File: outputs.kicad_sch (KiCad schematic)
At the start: 6 parts, among them U2 VNLD5160TR-E, U3 VNLD5160TR-E

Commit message: still initial layout
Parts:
- R3, R4, R5, R6: footprint (none) -> Resistor_SMD:R_0402_1005Metric
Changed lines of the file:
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@@
 			)
 		)
-		(property "Footprint" ""
+		(property "Footprint" "Resistor_SMD:R_0402_1005Metric"
 			(at 40.64 95.25 0)
 			(effects
@@
 			)
 		)
-		(property "Footprint" ""
+		(property "Footprint" "Resistor_SMD:R_0402_1005Metric"
 			(at 40.64 55.88 0)
 			(effects
@@
 			)
 		)
-		(property "Footprint" ""
+		(property "Footprint" "Resistor_SMD:R_0402_1005Metric"
 			(at 40.64 105.41 0)
 			(effects
@@
 			)
 		)
-		(property "Footprint" ""
+		(property "Footprint" "Resistor_SMD:R_0402_1005Metric"
 			(at 40.64 45.72 0)
 			(effects

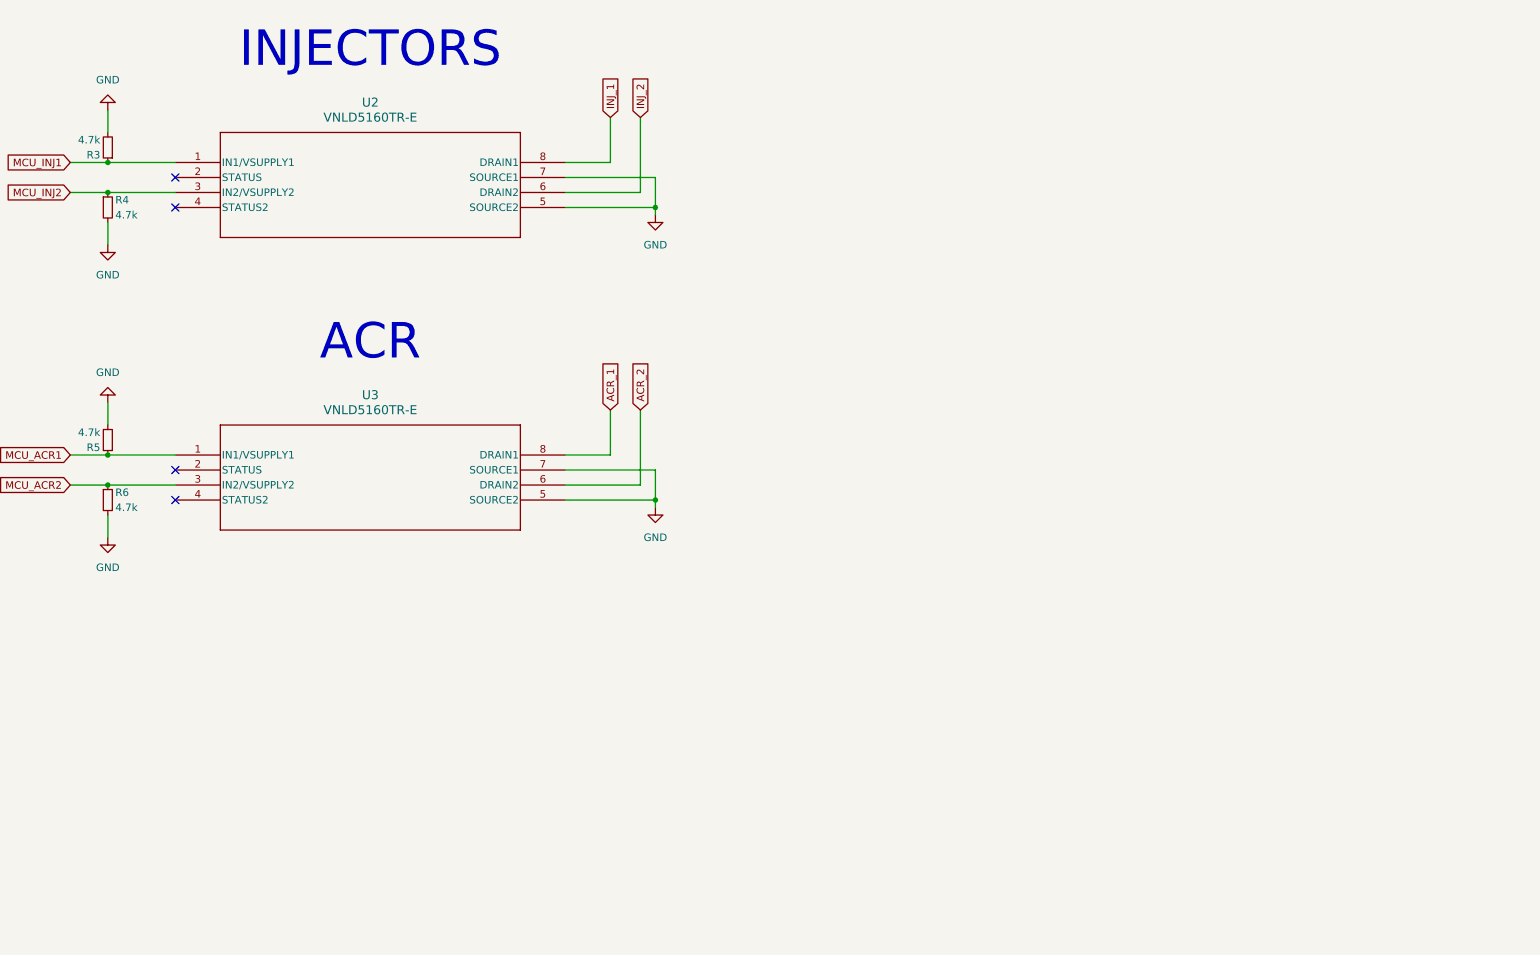
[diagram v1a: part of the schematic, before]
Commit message: igntion igbt, cooling mosfet
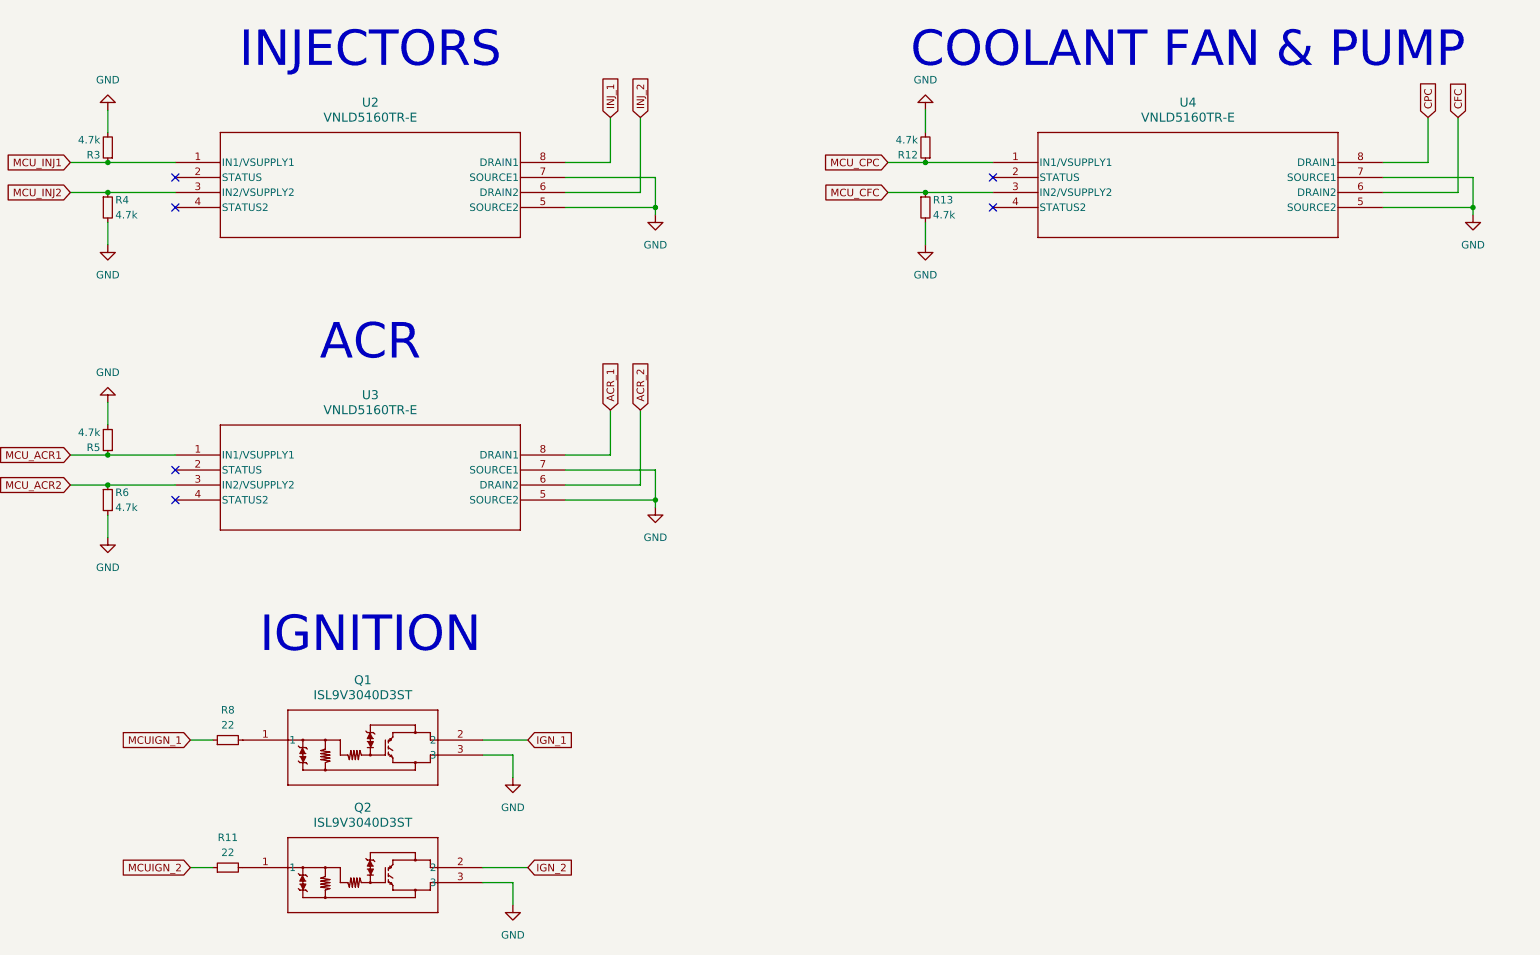
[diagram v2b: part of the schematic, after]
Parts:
- added Q1, Q2: ISL9V3040D3ST, TO-252AA_ONS, symbol ISL9V3040D3ST:ISL9V3040D3ST
- added R11, R8: 22, Resistor_SMD:R_0603_1608Metric, symbol Device:R_Small
- added R12, R13: 4.7k, Resistor_SMD:R_0402_1005Metric, symbol Device:R_Small
- added U4: VNLD5160TR-E, VNLD5160TR-E:SO_160TR-E_STM, symbol VNLD5160TR-E:VNLD5160TR-E
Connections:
- net GND: now also Q1.3, Q2.3, R12.2, R13.2, U4.5 (SOURCE2), U4.7 (SOURCE1)
- new net: Q2.1, R11.2
- new net: Q1.1, R8.2
- new net CFC: U4.6 (DRAIN2)
- new net CPC: U4.8 (DRAIN1)
- new net IGN_1: Q1.2
- new net IGN_2: Q2.2
- new net MCUIGN_1: R8.1
- new net MCUIGN_2: R11.1
- new net MCU_CFC: R13.1, U4.3 (IN2/VSUPPLY2)
- new net MCU_CPC: R12.1, U4.1 (IN1/VSUPPLY1)
- no-connect marks 4 -> 6
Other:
- note added: "COOLANT FAN & PUMP"
- note added: "IGNITION"

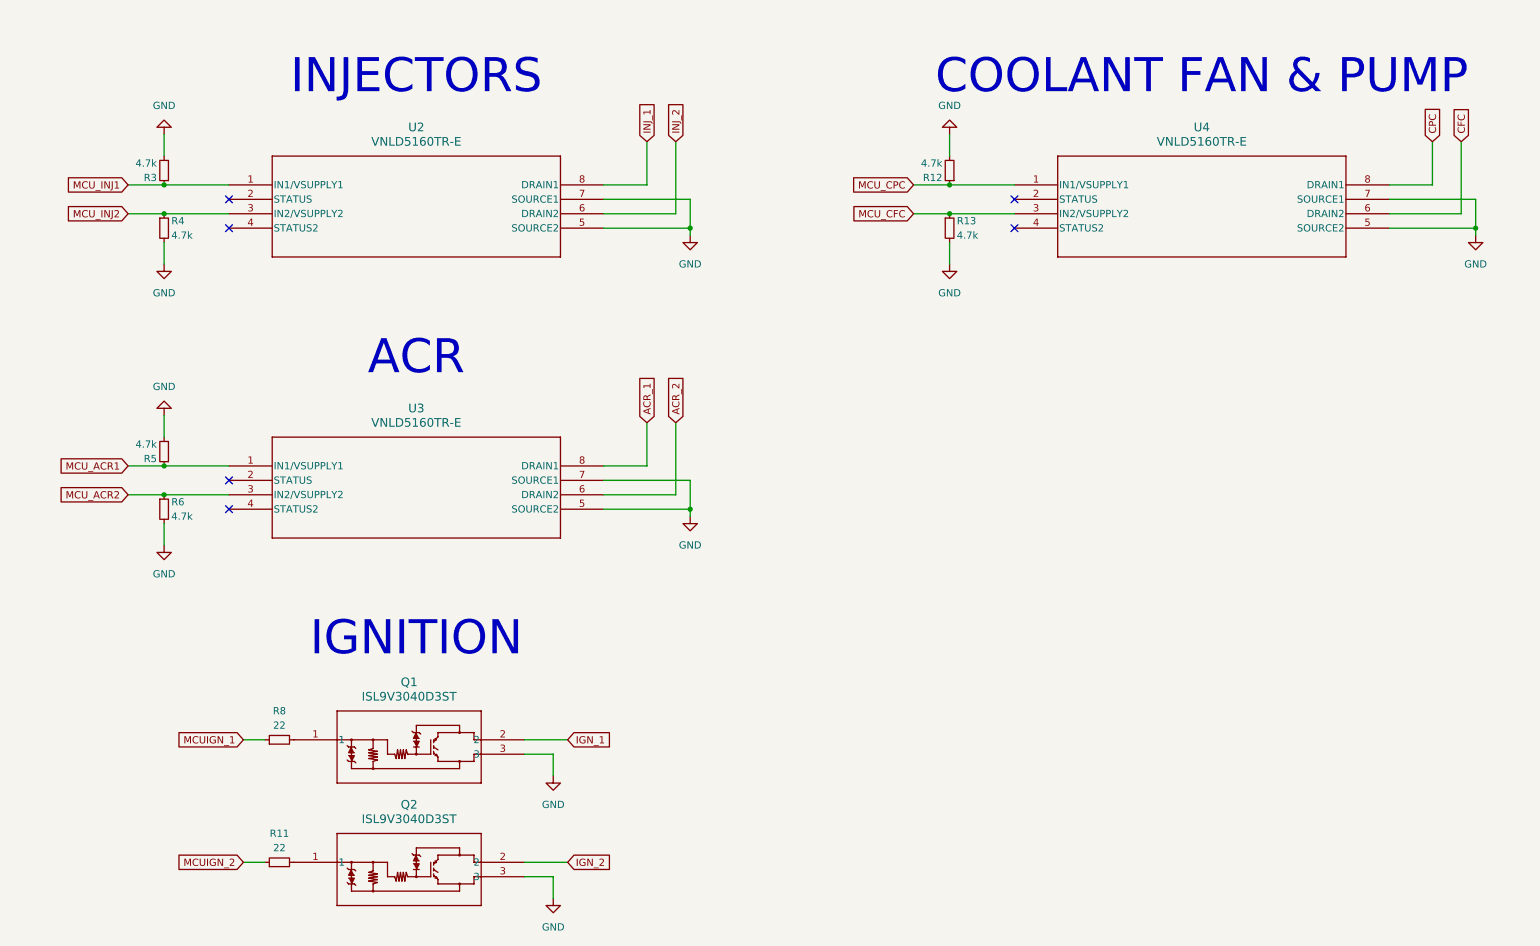
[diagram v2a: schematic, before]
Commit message: adding electronic throttle control
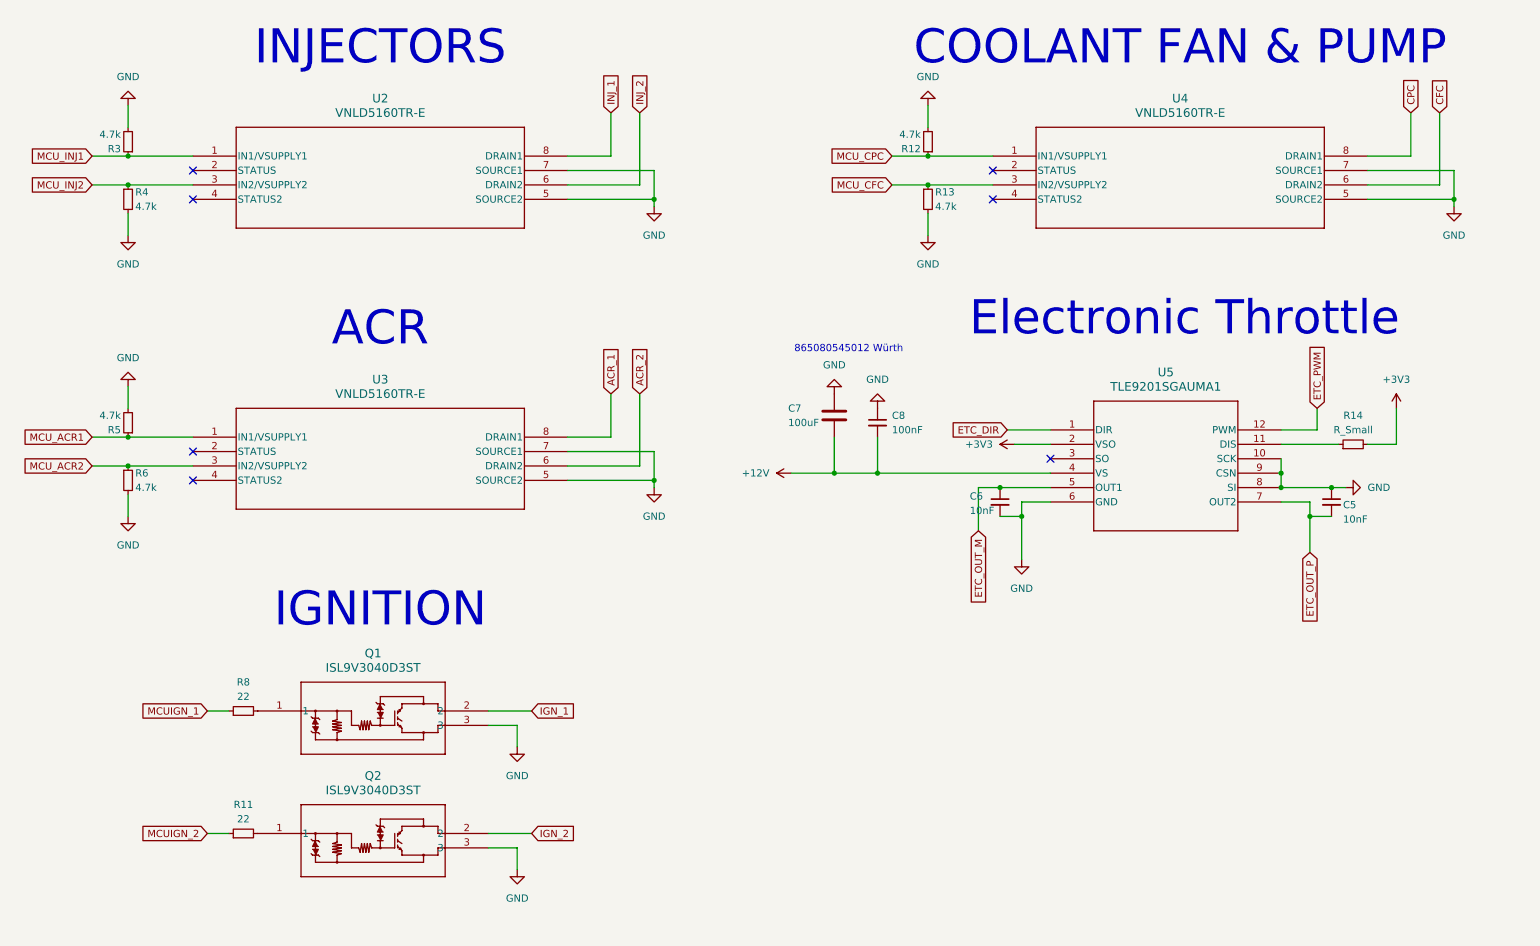
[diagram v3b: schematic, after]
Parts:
- added C5, C6: 10nF, Capacitor_SMD:C_0402_1005Metric, symbol Device:C_Small
- added C7: 100uF, Capacitor_SMD:C_Elec_6.3x5.8, symbol Device:C
- added C8: 100nF, Capacitor_SMD:C_0603_1608Metric, symbol Device:C_Small
- added R14: R_Small, symbol Device:R_Small
- added U5: TLE9201SGAUMA1, TLE9201SG:TLE9201SGAUMA1_INF, symbol TLE9201SG:TLE9201SGAUMA1
- Q1, Q2: footprint TO-252AA_ONS -> ISL9V3040D3ST:TO-252AA_ONS
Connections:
- net GND: now also C5.1, C6.2, C7.1, C8.1, U5.10 (SCK), U5.6 (GND), U5.8 (SI), U5.9 (CSN)
- new net: R14.1, U5.11 (DIS)
- new net +12V: C7.2, C8.2, U5.4 (VS)
- new net +3V3: R14.2, U5.2 (VSO)
- new net ETC_DIR: U5.1 (DIR)
- new net ETC_OUT_M: C6.1, U5.5 (OUT1)
- new net ETC_OUT_P: C5.2, U5.7 (OUT2)
- new net ETC_PWM: U5.12 (PWM)
- no-connect marks 6 -> 7
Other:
- note added: "865080545012 Würth"
- note added: "Electronic Throttle"
- moved on the sheet: Q1, Q2, R11, R12, R13, R3, R4, R5, R6, R8, U2, U3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

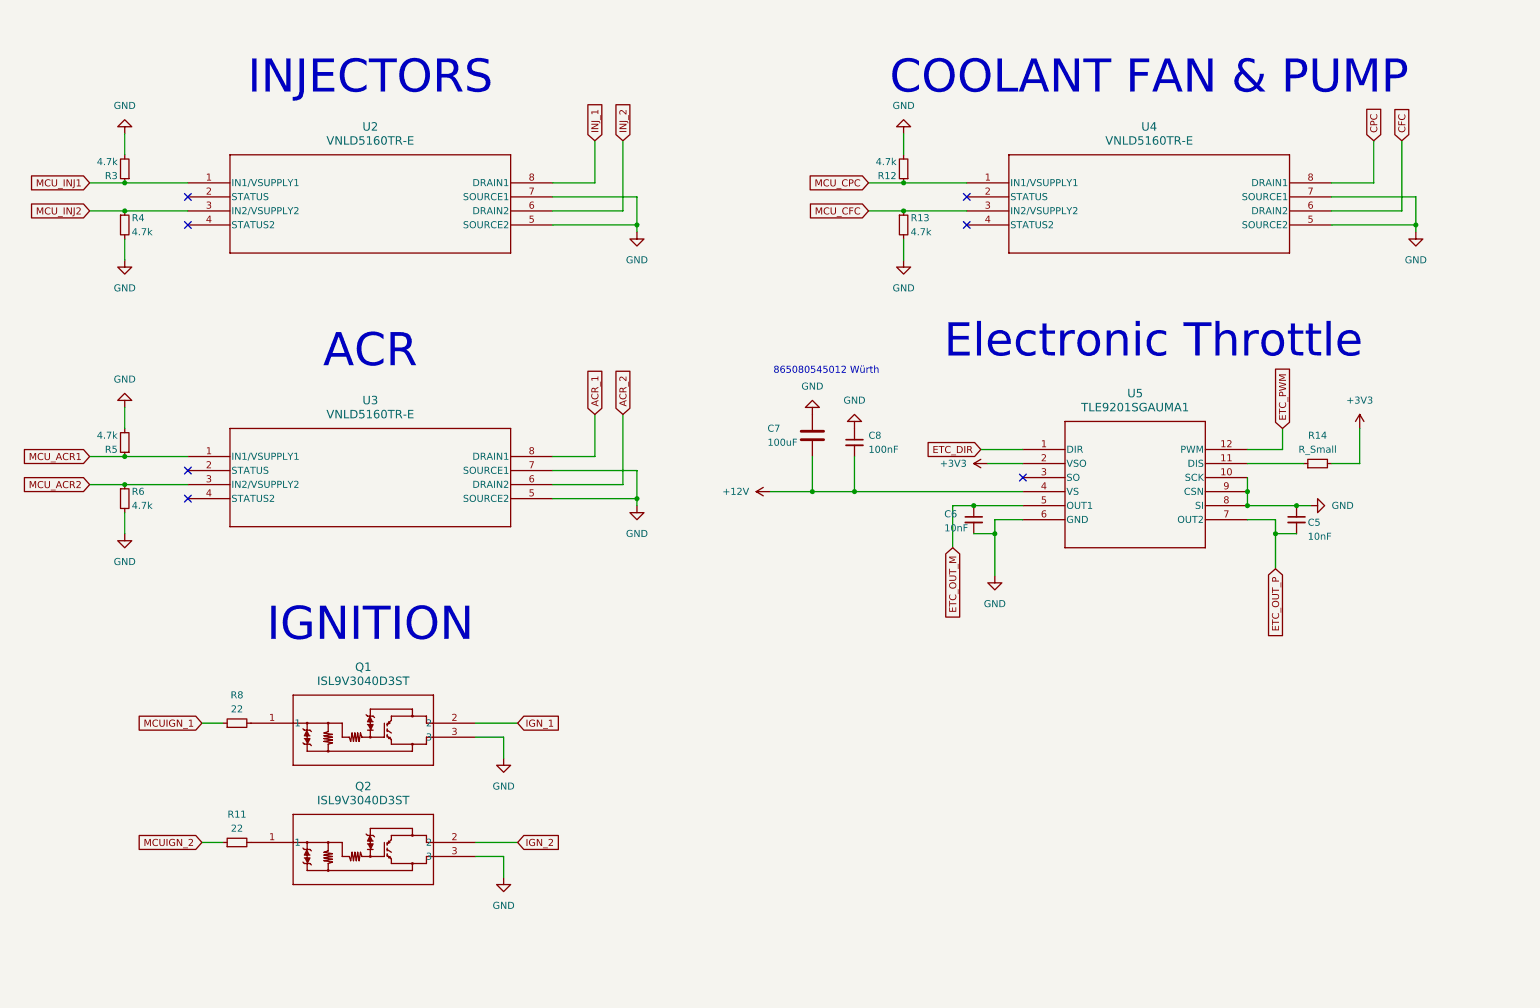
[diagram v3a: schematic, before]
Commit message: adding most remaining outputs and sensors like vvt, cam etc
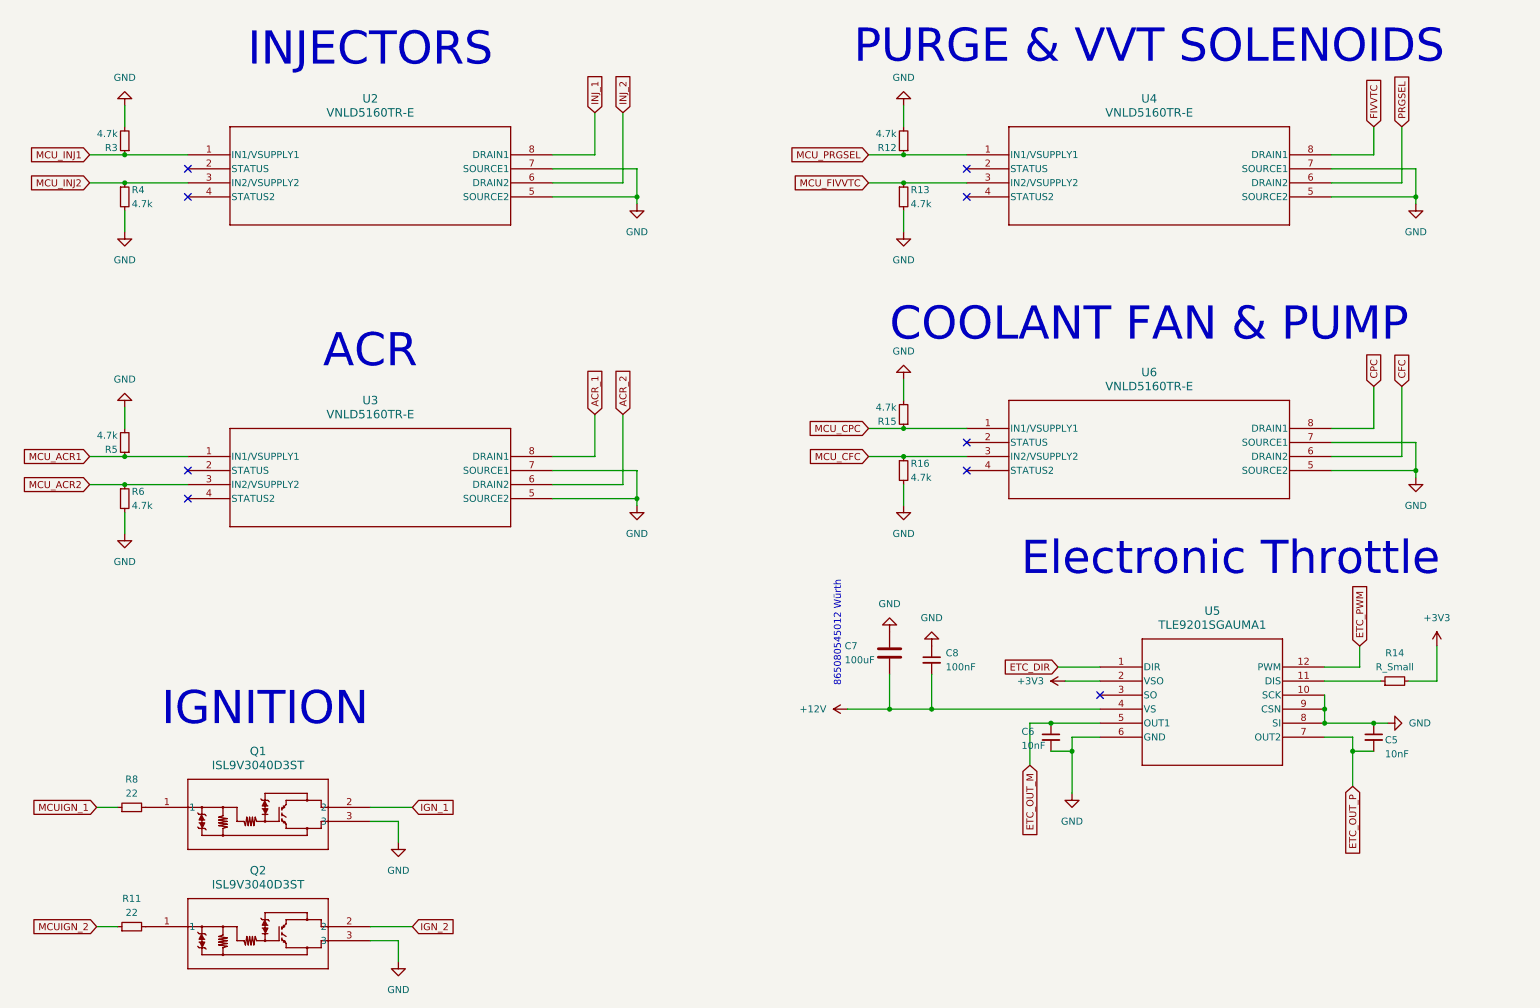
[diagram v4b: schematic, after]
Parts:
- added R15, R16: 4.7k, Resistor_SMD:R_0402_1005Metric, symbol Device:R_Small
- added U6: VNLD5160TR-E, VNLD5160TR-E:SO_160TR-E_STM, symbol VNLD5160TR-E:VNLD5160TR-E
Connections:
- net CFC: now also U6.6 (DRAIN2); no longer U4.6 (DRAIN2)
- net CPC: now also U6.8 (DRAIN1); no longer U4.8 (DRAIN1)
- net GND: now also R15.2, R16.2, U6.5 (SOURCE2), U6.7 (SOURCE1)
- net MCU_CFC: now also R16.1, U6.3 (IN2/VSUPPLY2); no longer R13.1, U4.3 (IN2/VSUPPLY2)
- net MCU_CPC: now also R15.1, U6.1 (IN1/VSUPPLY1); no longer R12.1, U4.1 (IN1/VSUPPLY1)
- new net FIVVTC: U4.8 (DRAIN1)
- new net MCU_FIVVTC: R13.1, U4.3 (IN2/VSUPPLY2)
- new net MCU_PRGSEL: R12.1, U4.1 (IN1/VSUPPLY1)
- new net PRGSEL: U4.6 (DRAIN2)
- no-connect marks 7 -> 9
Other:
- note added: "PURGE & VVT SOLENOIDS"
- moved on the sheet: C5, C6, C7, C8, Q1, Q2, R11, R12, R13, R14, R3, R4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
